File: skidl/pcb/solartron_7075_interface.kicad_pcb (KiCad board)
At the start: 4 copper layers, 112 x 44 mm, 94 parts, among them J1 DD-50 plug, J2 USB_B, J3 SWD, Q1 2N7002, SW1 BOOTSEL, SW2 RESET, U1 RP2354A, U10 74HCT165, U11 74HCT165, U12 74HCT165, U13 74HCT165, U14 74HCT165, U15 74HC595, U16 74HC595, U2 AP2112K-3.3, U3 USBLC6-2SC6, U4 78L05, U5 TLP2361, U6 TLP2361, U7 TLP2361, U8 TLP2361, U9 TLP2361, Y1 12MHz

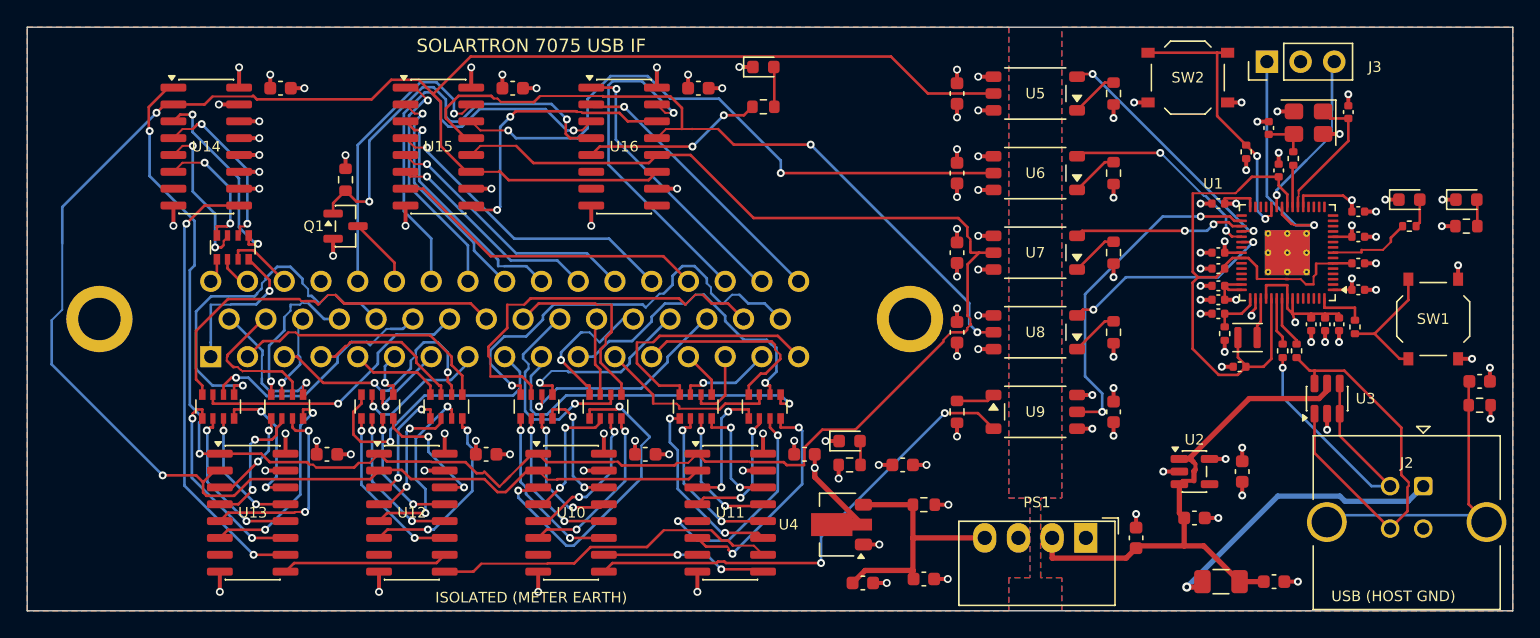
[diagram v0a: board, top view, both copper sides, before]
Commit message: skidl: tidy meter-side routing by pin swapping within parts
Reassign the D inputs of the 74HCT165s (U14's link-check inputs included),
the channels of the resistor arrays and the outputs of the 74HC595s, found by
scripts/optimise_pins.py (simulated annealing on straight-line crossings and
length; no part moved, no signal moved to another part). Re-routed with
Freerouting:

  arrays -> 74HCT165s: 64 -> 0 crossings, 441 -> 351 mm of track
  74HC595s -> J1:      36 -> 8 crossings, 265 -> 205 mm
  J1 -> arrays:       148 -> 102 crossings, 513 -> 481 mm
  whole board:        2428 -> 2227 mm of track, 262 -> 260 vias

DRC, ERC and schematic parity remain clean. The bit maps in the README and
the schematic notes (now generated from the netlist) follow the new
assignment; the link-check pattern is now 0011 on U14 D5..D2.

Co-Authored-By: Claude Opus 5.5 <noreply@anthropic.com>
Claude-Session: https://claude.ai/code/session_01ERGgANCwEg9niX4WLDjBj2
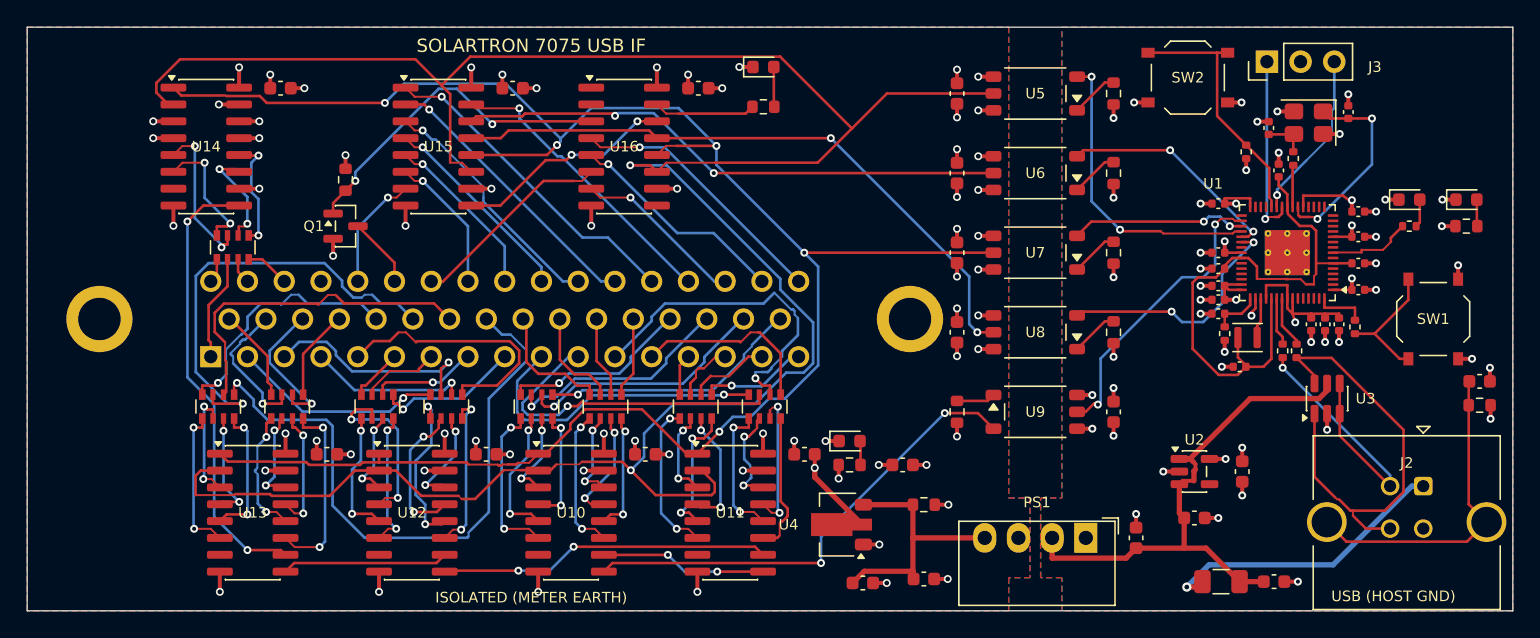
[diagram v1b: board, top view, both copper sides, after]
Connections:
- RN1 pad 1: /POL_POS -> /FUNC_OUT_B
- RN1 pad 2: /POL_NEG -> /FUNC_OUT_A
- RN1 pad 3: /FUNC_OUT_A -> /POL_NEG
- RN1 pad 4: /FUNC_OUT_B -> /POL_POS
- RN1 pad 5: /FUNC_OUT_B_R -> /POL_POS_R
- RN1 pad 6: /FUNC_OUT_A_R -> /POL_NEG_R
- RN1 pad 7: /POL_NEG_R -> /FUNC_OUT_A_R
- RN1 pad 8: /POL_POS_R -> /FUNC_OUT_B_R
- RN2 pad 1: /RANGE_OUT_4 -> /PRINT_PULSE
- RN2 pad 2: /RANGE_OUT_2 -> /RANGE_OUT_1
- RN2 pad 3: /RANGE_OUT_1 -> /RANGE_OUT_2
- RN2 pad 4: /PRINT_PULSE -> /RANGE_OUT_4
- RN2 pad 5: /PRINT_PULSE_R -> /RANGE_OUT_4_R
- RN2 pad 6: /RANGE_OUT_1_R -> /RANGE_OUT_2_R
- RN2 pad 7: /RANGE_OUT_2_R -> /RANGE_OUT_1_R
- RN2 pad 8: /RANGE_OUT_4_R -> /PRINT_PULSE_R
- RN3 pad 1: /BCD_1E3_8 -> /BCD_1E3_1
- RN3 pad 2: /BCD_1E3_4 -> /BCD_1E3_2
- RN3 pad 3: /BCD_1E3_2 -> /BCD_1E3_4
- RN3 pad 4: /BCD_1E3_1 -> /BCD_1E3_8
- RN3 pad 5: /BCD_1E3_1_R -> /BCD_1E3_8_R
- RN3 pad 6: /BCD_1E3_2_R -> /BCD_1E3_4_R
- RN3 pad 7: /BCD_1E3_4_R -> /BCD_1E3_2_R
- RN3 pad 8: /BCD_1E3_8_R -> /BCD_1E3_1_R
- RN4 pad 1: /BCD_1E2_8 -> /BCD_1E2_1
- RN4 pad 2: /BCD_1E2_4 -> /BCD_1E2_2
- RN4 pad 3: /BCD_1E2_2 -> /BCD_1E2_4
- RN4 pad 4: /BCD_1E2_1 -> /BCD_1E2_8
- RN4 pad 5: /BCD_1E2_1_R -> /BCD_1E2_8_R
- RN4 pad 6: /BCD_1E2_2_R -> /BCD_1E2_4_R
- RN4 pad 7: /BCD_1E2_4_R -> /BCD_1E2_2_R
- RN4 pad 8: /BCD_1E2_8_R -> /BCD_1E2_1_R
- RN5 pad 1: /BCD_1E5_8 -> /BCD_1E5_1
- RN5 pad 2: /BCD_1E5_4 -> /BCD_1E5_2
- RN5 pad 3: /BCD_1E5_2 -> /BCD_1E5_4
- RN5 pad 4: /BCD_1E5_1 -> /BCD_1E5_8
- RN5 pad 5: /BCD_1E5_1_R -> /BCD_1E5_8_R
- RN5 pad 6: /BCD_1E5_2_R -> /BCD_1E5_4_R
- RN5 pad 7: /BCD_1E5_4_R -> /BCD_1E5_2_R
- RN5 pad 8: /BCD_1E5_8_R -> /BCD_1E5_1_R
- RN6 pad 1: /BCD_1E4_8 -> /BCD_1E4_1
- RN6 pad 2: /BCD_1E4_4 -> /BCD_1E4_2
- RN6 pad 3: /BCD_1E4_2 -> /BCD_1E4_4
- RN6 pad 4: /BCD_1E4_1 -> /BCD_1E4_8
- RN6 pad 5: /BCD_1E4_1_R -> /BCD_1E4_8_R
- RN6 pad 6: /BCD_1E4_2_R -> /BCD_1E4_4_R
- RN6 pad 7: /BCD_1E4_4_R -> /BCD_1E4_2_R
- RN6 pad 8: /BCD_1E4_8_R -> /BCD_1E4_1_R
- RN7 pad 1: /BCD_1E1_8 -> /BCD_1E1_1
- RN7 pad 2: /BCD_1E1_4 -> /BCD_1E1_2
- RN7 pad 3: /BCD_1E1_2 -> /BCD_1E1_4
- RN7 pad 4: /BCD_1E1_1 -> /BCD_1E1_8
- RN7 pad 5: /BCD_1E1_1_R -> /BCD_1E1_8_R
- RN7 pad 6: /BCD_1E1_2_R -> /BCD_1E1_4_R
- RN7 pad 7: /BCD_1E1_4_R -> /BCD_1E1_2_R
- RN7 pad 8: /BCD_1E1_8_R -> /BCD_1E1_1_R
- RN8 pad 1: /BCD_1E0_8 -> /BCD_1E0_1
- RN8 pad 2: /BCD_1E0_4 -> /BCD_1E0_2
- RN8 pad 3: /BCD_1E0_2 -> /BCD_1E0_4
- RN8 pad 4: /BCD_1E0_1 -> /BCD_1E0_8
- RN8 pad 5: /BCD_1E0_1_R -> /BCD_1E0_8_R
- RN8 pad 6: /BCD_1E0_2_R -> /BCD_1E0_4_R
- RN8 pad 7: /BCD_1E0_4_R -> /BCD_1E0_2_R
- RN8 pad 8: /BCD_1E0_8_R -> /BCD_1E0_1_R
- RN9 pad 2: /DATA_CAN_CHANGE -> /BCD_1E6_1
- RN9 pad 3: /OVERLOAD -> /DATA_CAN_CHANGE
- RN9 pad 4: /BCD_1E6_1 -> /OVERLOAD
- RN9 pad 5: /BCD_1E6_1_R -> /OVERLOAD_R
- RN9 pad 6: /OVERLOAD_R -> /DATA_CAN_CHANGE_R
- RN9 pad 7: /DATA_CAN_CHANGE_R -> /BCD_1E6_1_R
- U10 pad 11: /PRINT_PULSE_R -> /POL_POS_R
- U10 pad 12: /RANGE_OUT_1_R -> /FUNC_OUT_B_R
- U10 pad 13: /RANGE_OUT_2_R -> /FUNC_OUT_A_R
- U10 pad 14: /RANGE_OUT_4_R -> /POL_NEG_R
- U10 pad 3: /FUNC_OUT_B_R -> /RANGE_OUT_1_R
- U10 pad 4: /FUNC_OUT_A_R -> /PRINT_PULSE_R
- U10 pad 5: /POL_NEG_R -> /RANGE_OUT_2_R
- U10 pad 6: /POL_POS_R -> /RANGE_OUT_4_R
- U11 pad 11: /BCD_1E2_1_R -> /BCD_1E3_1_R
- U11 pad 12: /BCD_1E2_2_R -> /BCD_1E3_8_R
- U11 pad 13: /BCD_1E2_4_R -> /BCD_1E3_2_R
- U11 pad 14: /BCD_1E2_8_R -> /BCD_1E3_4_R
- U11 pad 3: /BCD_1E3_1_R -> /BCD_1E2_4_R
- U11 pad 4: /BCD_1E3_2_R -> /BCD_1E2_2_R
- U11 pad 5: /BCD_1E3_4_R -> /BCD_1E2_1_R
- U11 pad 6: /BCD_1E3_8_R -> /BCD_1E2_8_R
- U12 pad 11: /BCD_1E4_1_R -> /BCD_1E5_1_R
- U12 pad 12: /BCD_1E4_2_R -> /BCD_1E5_8_R
- U12 pad 13: /BCD_1E4_4_R -> /BCD_1E5_4_R
- U12 pad 14: /BCD_1E4_8_R -> /BCD_1E5_2_R
- U12 pad 3: /BCD_1E5_1_R -> /BCD_1E4_2_R
- U12 pad 4: /BCD_1E5_2_R -> /BCD_1E4_4_R
- U12 pad 5: /BCD_1E5_4_R -> /BCD_1E4_8_R
- U12 pad 6: /BCD_1E5_8_R -> /BCD_1E4_1_R
- U13 pad 11: /BCD_1E0_1_R -> /BCD_1E1_1_R
- U13 pad 12: /BCD_1E0_2_R -> /BCD_1E1_8_R
- U13 pad 13: /BCD_1E0_4_R -> /BCD_1E1_2_R
- U13 pad 14: /BCD_1E0_8_R -> /BCD_1E1_4_R
- U13 pad 3: /BCD_1E1_1_R -> /BCD_1E0_4_R
- U13 pad 4: /BCD_1E1_2_R -> /BCD_1E0_2_R
- U13 pad 5: /BCD_1E1_4_R -> /BCD_1E0_1_R
- U13 pad 6: /BCD_1E1_8_R -> /BCD_1E0_8_R
- U14 pad 11: ISO_GND -> /DATA_CAN_CHANGE_R
- U14 pad 12: ISO_+5V -> /OVERLOAD_R
- U14 pad 13: ISO_GND -> ISO_+5V
- U14 pad 3: /BCD_1E6_1_R -> ISO_GND
- U14 pad 4: /OVERLOAD_R -> ISO_GND
- U14 pad 5: /DATA_CAN_CHANGE_R -> /BCD_1E6_1_R
- U15 pad 1: /RATIO_N -> /INTEG_1
- U15 pad 15: /LOCKOUT_N -> /AUTORANGE_INH
- U15 pad 2: /FUNC_CMD_42 -> /INTEG_2
- U15 pad 3: /FUNC_CMD_43 -> /INTEG_4
- U15 pad 4: /INTEG_1 -> /FUNC_CMD_43
- U15 pad 5: /INTEG_2 -> /FUNC_CMD_42
- U15 pad 6: /INTEG_4 -> /RATIO_N
- U15 pad 7: /AUTORANGE_INH -> /LOCKOUT_N
- U16 pad 1: /RANGE_CMD_2 -> unconnected-(U16-QB-Pad1)
- U16 pad 15: /RANGE_CMD_1 -> /LED_REMOTE
- U16 pad 2: /RANGE_CMD_4 -> unconnected-(U16-QC-Pad2)
- U16 pad 3: /SAMPLE_PULSE -> /SAMPLE_CONTACT_DRV
- U16 pad 4: /SAMPLE_CONTACT_DRV -> /RANGE_CMD_4
- U16 pad 5: /LED_REMOTE -> /RANGE_CMD_2
- U16 pad 6: unconnected-(U16-QG-Pad6) -> /SAMPLE_PULSE
- U16 pad 7: unconnected-(U16-QH-Pad7) -> /RANGE_CMD_1
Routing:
- net /ISO_SCLK: track 168.8 -> 187.0 mm
- net /BCD_1E0_1: track 29.1 -> 46.9 mm, vias 0 -> 1
- net /SAMPLE_PULSE: track 31.6 -> 15.5 mm, vias 1 -> 0
- net /FUNC_OUT_B_R: track 24.6 -> 9.08 mm
- net /BCD_1E0_4: track 18.7 -> 33.6 mm
- net /LOCKOUT_N: track 22.7 -> 8.87 mm
- net /BCD_1E5_1: track 7.06 -> 20.2 mm
- net /RANGE_CMD_1: track 26.0 -> 13.0 mm
- net /PRINT_PULSE: track 32.6 -> 19.8 mm
- net /BCD_1E3_2: track 13.9 -> 25.4 mm, vias 0 -> 1
- net /BCD_1E2_1: track 19.2 -> 8.19 mm, vias 0 -> 1
- net /RANGE_OUT_1: track 29.4 -> 18.9 mm, vias 0 -> 1
- net /BCD_1E4_1: track 21.1 -> 10.9 mm
- net /BCD_1E3_4_R: track 16.9 -> 7.71 mm
- net /POL_NEG: track 16.3 -> 7.60 mm, vias 1 -> 0
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
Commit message: skidl: swap pins between parts and move the meter-side registers
scripts/optimise_layout.py extends the pin-swap search across parts (any
meter output on any array channel and 74HCT165 input, any command input on
any 74HC595 output) and lets the registers change places and turn 180
degrees; it also scores the clock, latch, /OE, MOSI and chain nets. Result:
all seven registers turned 180 degrees (control and supply pins away from J1
and the arrays), the 74HCT165s in chain order along the bottom row, U15/U16
swapped, decoupling caps moved with the supply pins. Re-routed:

  J1 -> arrays:     102 -> 10 crossings, 481 -> 255 mm of track, 18 -> 6 vias
  74HC595s -> J1:     8 -> 1 crossing,   205 -> 137 mm, 11 -> 7 vias
  control + chains:                      558 -> 494 mm
  whole board:      2227 -> 1868 mm of track, 260 -> 243 vias

DRC, ERC and schematic parity are clean. README bit maps and the routing
review section are updated; the link check is now 1010 on U14 D3..D0.

Co-Authored-By: Claude Opus 5.5 <noreply@anthropic.com>
Claude-Session: https://claude.ai/code/session_01ERGgANCwEg9niX4WLDjBj2
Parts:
- moved C32 25.0 mm to (28.5, 16.3), turned to -90 degrees
- moved C27 24.8 mm to (35.4, 41.0), turned to 180 degrees
- moved C29 14.2 mm to (11.4, 41.0), turned to 180 degrees
- moved C28 14.2 mm to (23.4, 41.0), turned to 180 degrees
- moved C30 14.2 mm to (11.0, 16.3), turned to -90 degrees
- moved U15 14.0 mm to (45.0, 9.00), turned to 180 degrees
- moved U16 14.0 mm to (31.0, 9.00), turned to 180 degrees
- moved C31 13.1 mm to (42.5, 16.3), turned to -90 degrees
- moved U10 12.0 mm to (53.0, 36.6), turned to 180 degrees
- moved U11 12.0 mm to (41.0, 36.6), turned to 180 degrees
- moved C26 8.84 mm to (47.4, 41.0), turned to 180 degrees
- turned U12 to 180 degrees
- turned U13 to 180 degrees
- turned U14 to 180 degrees
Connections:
- RN1 pad 1: /FUNC_OUT_B -> /RANGE_OUT_2
- RN1 pad 2: /FUNC_OUT_A -> /FUNC_OUT_B
- RN1 pad 4: /POL_POS -> /FUNC_OUT_A
- RN1 pad 5: /POL_POS_R -> /FUNC_OUT_A_R
- RN1 pad 7: /FUNC_OUT_A_R -> /FUNC_OUT_B_R
- RN1 pad 8: /FUNC_OUT_B_R -> /RANGE_OUT_2_R
- RN2 pad 1: /PRINT_PULSE -> /BCD_1E3_4
- RN2 pad 2: /RANGE_OUT_1 -> /BCD_1E3_8
- RN2 pad 3: /RANGE_OUT_2 -> /POL_POS
- RN2 pad 4: /RANGE_OUT_4 -> /BCD_1E4_1
- RN2 pad 5: /RANGE_OUT_4_R -> /BCD_1E4_1_R
- RN2 pad 6: /RANGE_OUT_2_R -> /POL_POS_R
- RN2 pad 7: /RANGE_OUT_1_R -> /BCD_1E3_8_R
- RN2 pad 8: /PRINT_PULSE_R -> /BCD_1E3_4_R
- RN3 pad 1: /BCD_1E3_1 -> /BCD_1E2_1
- RN3 pad 2: /BCD_1E3_2 -> /PRINT_PULSE
- RN3 pad 3: /BCD_1E3_4 -> /BCD_1E2_2
- RN3 pad 4: /BCD_1E3_8 -> /RANGE_OUT_1
- RN3 pad 5: /BCD_1E3_8_R -> /RANGE_OUT_1_R
- RN3 pad 6: /BCD_1E3_4_R -> /BCD_1E2_2_R
- RN3 pad 7: /BCD_1E3_2_R -> /PRINT_PULSE_R
- RN3 pad 8: /BCD_1E3_1_R -> /BCD_1E2_1_R
- RN4 pad 1: /BCD_1E2_1 -> /BCD_1E2_4
- RN4 pad 2: /BCD_1E2_2 -> /BCD_1E2_8
- RN4 pad 3: /BCD_1E2_4 -> /RANGE_OUT_4
- RN4 pad 4: /BCD_1E2_8 -> /BCD_1E3_2
- RN4 pad 5: /BCD_1E2_8_R -> /BCD_1E3_2_R
- RN4 pad 6: /BCD_1E2_4_R -> /RANGE_OUT_4_R
- RN4 pad 7: /BCD_1E2_2_R -> /BCD_1E2_8_R
- RN4 pad 8: /BCD_1E2_1_R -> /BCD_1E2_4_R
- RN5 pad 1: /BCD_1E5_1 -> /BCD_1E0_1
- RN5 pad 2: /BCD_1E5_2 -> /BCD_1E4_2
- RN5 pad 3: /BCD_1E5_4 -> /BCD_1E4_4
- RN5 pad 4: /BCD_1E5_8 -> /BCD_1E0_4
- RN5 pad 5: /BCD_1E5_8_R -> /BCD_1E0_4_R
- RN5 pad 6: /BCD_1E5_4_R -> /BCD_1E4_4_R
- RN5 pad 7: /BCD_1E5_2_R -> /BCD_1E4_2_R
- RN5 pad 8: /BCD_1E5_1_R -> /BCD_1E0_1_R
- RN6 pad 1: /BCD_1E4_1 -> /BCD_1E4_8
- RN6 pad 2: /BCD_1E4_2 -> /BCD_1E0_8
- RN6 pad 3: /BCD_1E4_4 -> /BCD_1E1_1
- RN6 pad 4: /BCD_1E4_8 -> /DATA_CAN_CHANGE
- RN6 pad 5: /BCD_1E4_8_R -> /DATA_CAN_CHANGE_R
- RN6 pad 6: /BCD_1E4_4_R -> /BCD_1E1_1_R
- RN6 pad 7: /BCD_1E4_2_R -> /BCD_1E0_8_R
- RN6 pad 8: /BCD_1E4_1_R -> /BCD_1E4_8_R
- RN7 pad 1: /BCD_1E1_1 -> /BCD_1E5_2
- RN7 pad 3: /BCD_1E1_4 -> /BCD_1E5_4
- RN7 pad 4: /BCD_1E1_8 -> /BCD_1E1_4
- RN7 pad 5: /BCD_1E1_8_R -> /BCD_1E1_4_R
- RN7 pad 6: /BCD_1E1_4_R -> /BCD_1E5_4_R
- RN7 pad 8: /BCD_1E1_1_R -> /BCD_1E5_2_R
- RN8 pad 1: /BCD_1E0_1 -> /BCD_1E5_8
- RN8 pad 2: /BCD_1E0_2 -> /BCD_1E1_8
- RN8 pad 3: /BCD_1E0_4 -> /BCD_1E6_1
- RN8 pad 4: /BCD_1E0_8 -> /PRINT_LEVEL
- RN8 pad 5: /BCD_1E0_8_R -> /PRINT_LEVEL_R
- RN8 pad 6: /BCD_1E0_4_R -> /BCD_1E6_1_R
- RN8 pad 7: /BCD_1E0_2_R -> /BCD_1E1_8_R
- RN8 pad 8: /BCD_1E0_1_R -> /BCD_1E5_8_R
- RN9 pad 1: /PRINT_LEVEL -> /BCD_1E5_1
- RN9 pad 2: /BCD_1E6_1 -> /OVERLOAD
- RN9 pad 3: /DATA_CAN_CHANGE -> /BCD_1E0_2
- RN9 pad 4: /OVERLOAD -> /BCD_1E3_1
- RN9 pad 5: /OVERLOAD_R -> /BCD_1E3_1_R
- RN9 pad 6: /DATA_CAN_CHANGE_R -> /BCD_1E0_2_R
- RN9 pad 7: /BCD_1E6_1_R -> /OVERLOAD_R
- RN9 pad 8: /PRINT_LEVEL_R -> /BCD_1E5_1_R
- U10 pad 11: /POL_POS_R -> /BCD_1E2_8_R
- U10 pad 12: /FUNC_OUT_B_R -> /BCD_1E2_4_R
- U10 pad 13: /FUNC_OUT_A_R -> /RANGE_OUT_4_R
- U10 pad 14: /POL_NEG_R -> /BCD_1E3_2_R
- U10 pad 3: /RANGE_OUT_1_R -> /BCD_1E2_1_R
- U10 pad 4: /PRINT_PULSE_R -> /RANGE_OUT_1_R
- U10 pad 5: /RANGE_OUT_2_R -> /PRINT_PULSE_R
- U10 pad 6: /RANGE_OUT_4_R -> /BCD_1E2_2_R
- U11 pad 11: /BCD_1E3_1_R -> /BCD_1E3_8_R
- U11 pad 12: /BCD_1E3_8_R -> /POL_POS_R
- U11 pad 13: /BCD_1E3_2_R -> /BCD_1E3_4_R
- U11 pad 14: /BCD_1E3_4_R -> /BCD_1E4_1_R
- U11 pad 3: /BCD_1E2_4_R -> /FUNC_OUT_A_R
- U11 pad 4: /BCD_1E2_2_R -> /RANGE_OUT_2_R
- U11 pad 5: /BCD_1E2_1_R -> /POL_NEG_R
- U11 pad 6: /BCD_1E2_8_R -> /FUNC_OUT_B_R
- U12 pad 11: /BCD_1E5_1_R -> /BCD_1E1_1_R
- U12 pad 12: /BCD_1E5_8_R -> /BCD_1E0_8_R
- U12 pad 13: /BCD_1E5_4_R -> /BCD_1E4_8_R
- U12 pad 14: /BCD_1E5_2_R -> /DATA_CAN_CHANGE_R
- U12 pad 3: /BCD_1E4_2_R -> /BCD_1E0_1_R
- U12 pad 4: /BCD_1E4_4_R -> /BCD_1E0_4_R
- U12 pad 5: /BCD_1E4_8_R -> /BCD_1E4_2_R
- U12 pad 6: /BCD_1E4_1_R -> /BCD_1E4_4_R
- U13 pad 11: /BCD_1E1_1_R -> /BCD_1E6_1_R
- U13 pad 13: /BCD_1E1_2_R -> /BCD_1E5_8_R
- U13 pad 14: /BCD_1E1_4_R -> /PRINT_LEVEL_R
- U13 pad 3: /BCD_1E0_4_R -> /BCD_1E1_4_R
- U13 pad 4: /BCD_1E0_2_R -> /BCD_1E5_2_R
- U13 pad 5: /BCD_1E0_1_R -> /BCD_1E1_2_R
- U13 pad 6: /BCD_1E0_8_R -> /BCD_1E5_4_R
- U14 pad 11: /DATA_CAN_CHANGE_R -> ISO_GND
- U14 pad 12: /OVERLOAD_R -> ISO_+5V
- U14 pad 13: ISO_+5V -> ISO_GND
- U14 pad 3: ISO_GND -> /BCD_1E0_2_R
- U14 pad 4: ISO_GND -> /OVERLOAD_R
- U14 pad 5: /BCD_1E6_1_R -> /BCD_1E3_1_R
- U14 pad 6: /PRINT_LEVEL_R -> /BCD_1E5_1_R
- U15 pad 15: /AUTORANGE_INH -> /INTEG_4
- U15 pad 2: /INTEG_2 -> /AUTORANGE_INH
- U15 pad 3: /INTEG_4 -> /INTEG_2
- U15 pad 4: /FUNC_CMD_43 -> /RANGE_CMD_1
- U15 pad 5: /FUNC_CMD_42 -> /RANGE_CMD_2
- U15 pad 6: /RATIO_N -> /RANGE_CMD_4
- U15 pad 7: /LOCKOUT_N -> /LED_REMOTE
- U16 pad 1: unconnected-(U16-QB-Pad1) -> /RATIO_N
- U16 pad 15: /LED_REMOTE -> /SAMPLE_CONTACT_DRV
- U16 pad 2: unconnected-(U16-QC-Pad2) -> /FUNC_CMD_42
- U16 pad 3: /SAMPLE_CONTACT_DRV -> /SAMPLE_PULSE
- U16 pad 4: /RANGE_CMD_4 -> /FUNC_CMD_43
- U16 pad 5: /RANGE_CMD_2 -> /LOCKOUT_N
- U16 pad 6: /SAMPLE_PULSE -> unconnected-(U16-QG-Pad6)
- U16 pad 7: /RANGE_CMD_1 -> unconnected-(U16-QH-Pad7)
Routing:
- net /ISO_SCLK: track 187.0 -> 141.9 mm
- net /BCD_1E0_1: track 46.9 -> 6.45 mm, vias 1 -> 0
- net /BCD_1E0_4: track 33.6 -> 6.25 mm, vias 1 -> 0
- net /BCD_1E3_8: track 23.4 -> 2.87 mm, vias 1 -> 0
- net /BCD_1E3_1: track 14.3 -> 34.4 mm, vias 0 -> 1
- net /BCD_1E3_4: track 25.3 -> 5.64 mm
- net /BCD_1E3_2: track 25.4 -> 6.47 mm
- net /INTEG_1: track 24.6 -> 5.88 mm
- net /SAMPLE_CONTACT_DRV: track 25.4 -> 6.70 mm, vias 2 -> 0
- net /BCD_1E5_4: track 17.0 -> 2.93 mm, vias 1 -> 0
- net /PRINT_PULSE: track 19.8 -> 6.02 mm, vias 1 -> 0
- net /AUTORANGE_INH: track 22.3 -> 8.96 mm, vias 1 -> 0
- net /BCD_1E0_8: track 19.1 -> 5.91 mm, vias 1 -> 0
- net /RANGE_OUT_1: track 18.9 -> 5.86 mm, vias 1 -> 0
- net /BCD_1E5_8: track 16.0 -> 3.28 mm, vias 1 -> 0
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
